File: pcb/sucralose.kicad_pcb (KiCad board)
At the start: 2 copper layers, 154.3 x 89.9 mm, 98 parts, among them M1 MountingHole_1.2mm_M1

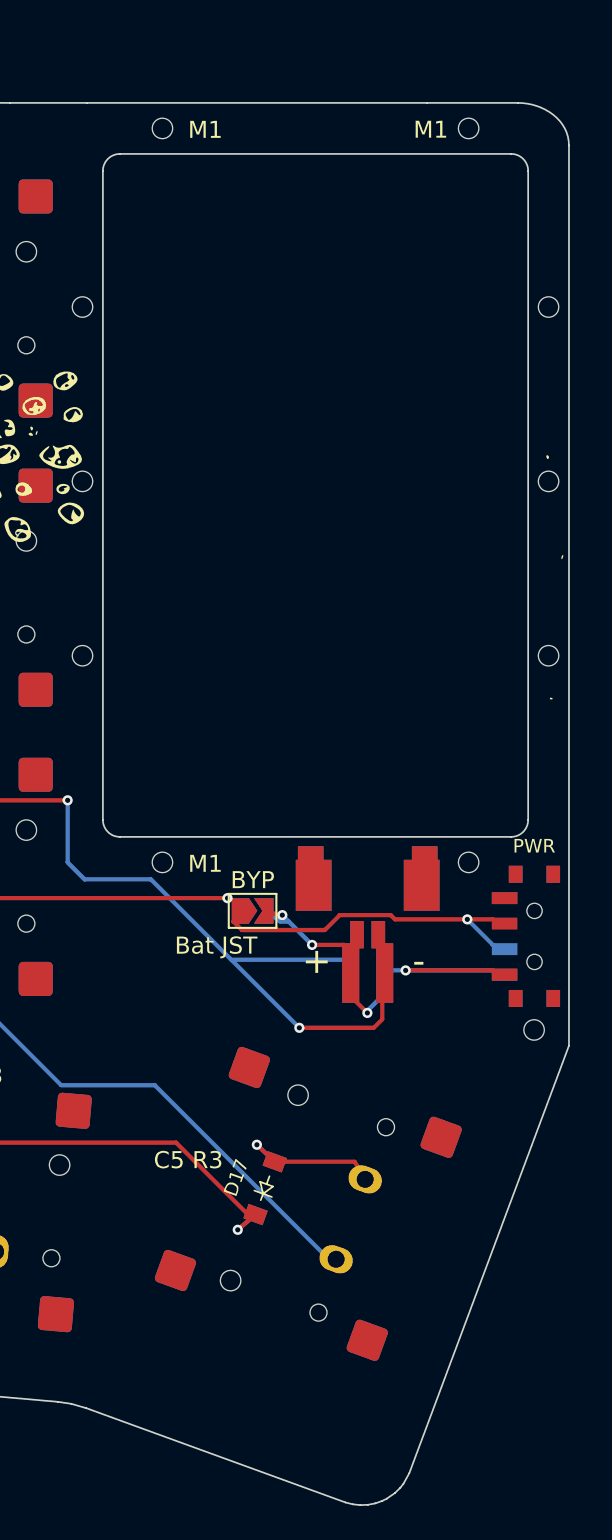
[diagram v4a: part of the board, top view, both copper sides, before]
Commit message: Battery bay cutout + 4 corner M1 holes +0.5 mm x. Right board edge, right-strip M1 holes (x 204.65), PWR switch F/B + its M1 and traces, right-strip silk art +0.5 mm with them; lower-right diagonal keeps its angle. All hole/edge gaps unchanged. DRC 362, same categories and unconnected set.
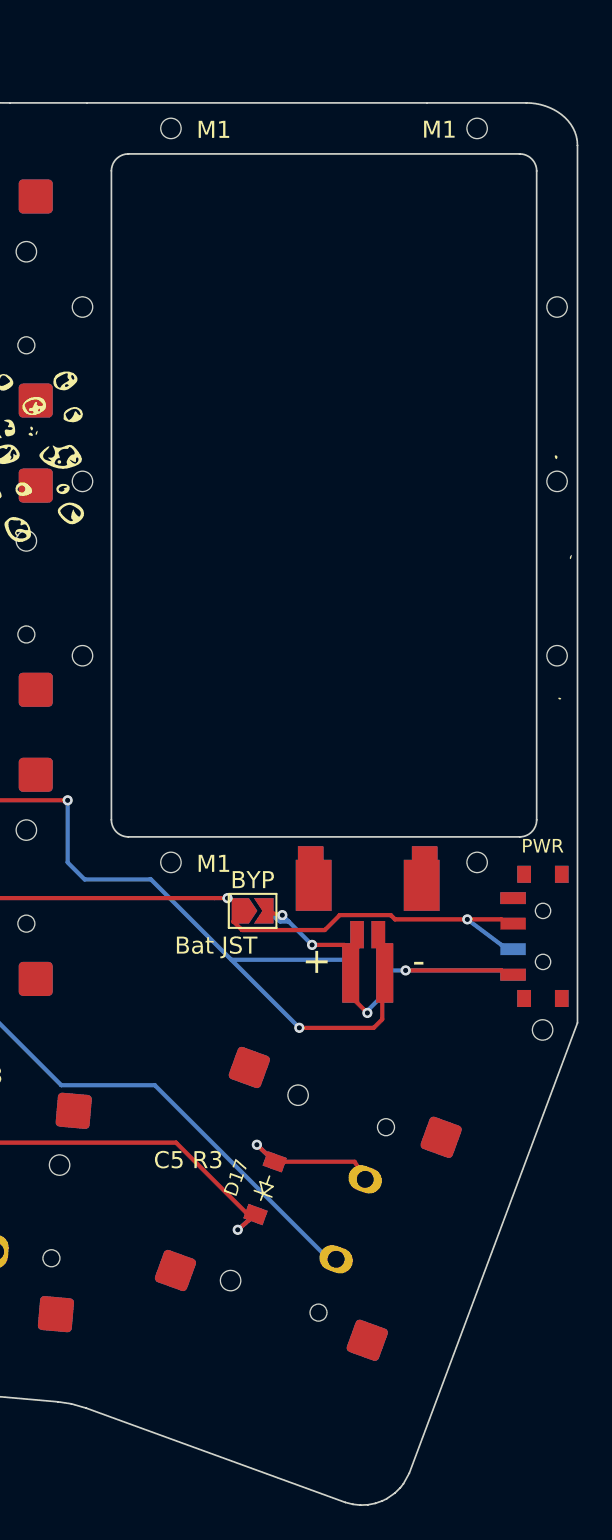
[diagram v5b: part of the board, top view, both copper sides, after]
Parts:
- moved M1 0.50 mm to (203.8, 111.0)
- moved M1 0.50 mm to (204.7, 68.5)
- moved M1 0.50 mm to (181.9, 58.0)
- moved M1 0.50 mm to (204.7, 89.0)
- moved M1 0.50 mm to (199.9, 101.2)
- moved M1 0.50 mm to (181.9, 101.2)
- moved M1 0.50 mm to (199.9, 58.0)
- moved M1 0.50 mm to (204.7, 78.8)
- moved PWR 0.50 mm to (203.8, 105.5) (x2)
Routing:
- net BAT_RAW: track 27.0 -> 28.0 mm
- net BAT_P: track 92.8 -> 93.6 mm
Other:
- board size 154.3 x 89.9 mm -> 154.8 x 89.9 mm

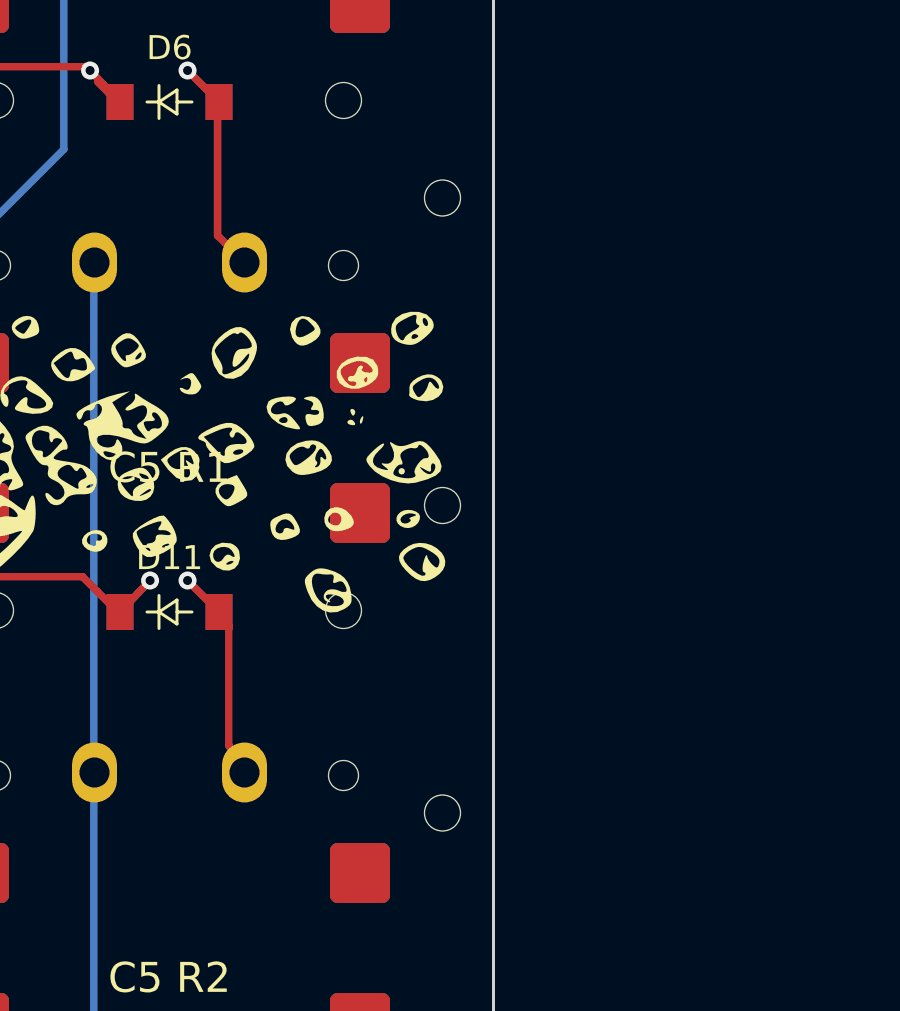
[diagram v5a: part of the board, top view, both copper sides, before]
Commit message: Left-strip battery-bay M1 holes (x 176.75 -> 177.25) +0.5 mm with the cutout; 1.2 mm to bay edge restored. DRC 362 unchanged.
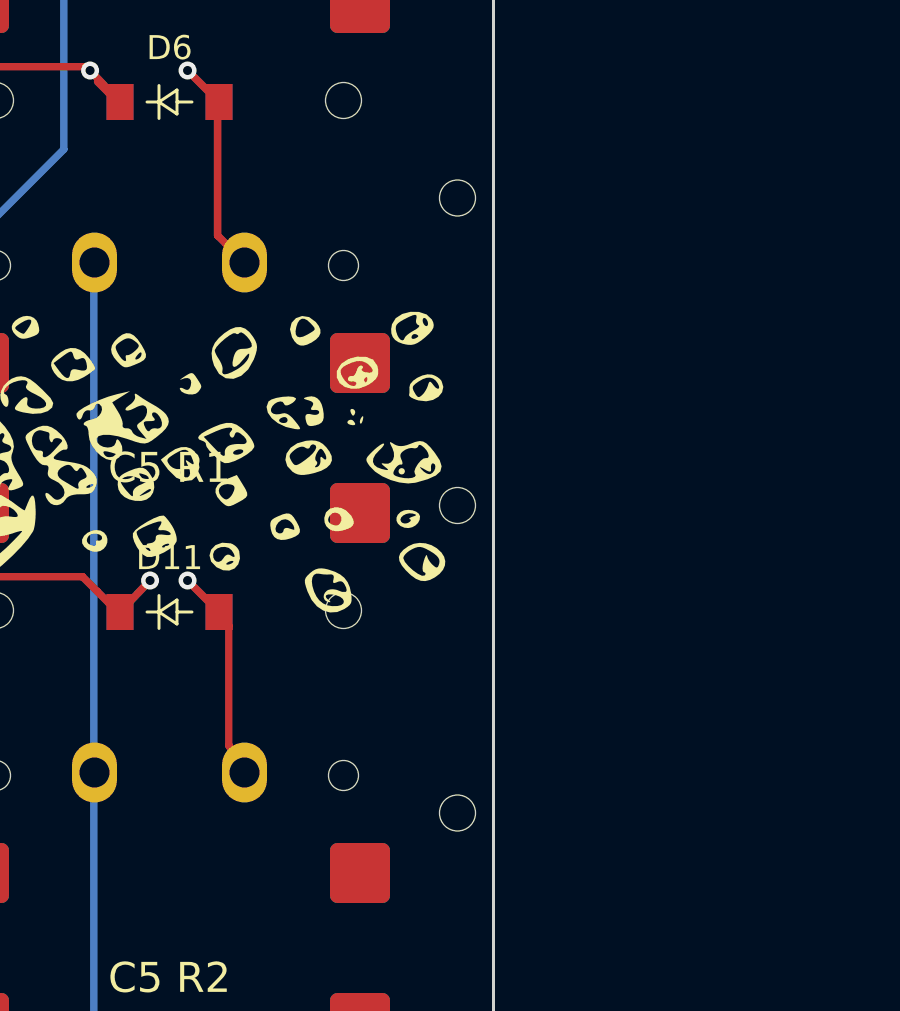
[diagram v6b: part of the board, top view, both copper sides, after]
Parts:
- moved M1 0.50 mm to (177.2, 78.8)
- moved M1 0.50 mm to (177.2, 89.0)
- moved M1 0.50 mm to (177.2, 68.5)
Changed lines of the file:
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@@
 	(footprint "CustomParts:MountingHole_1.2mm_M1"
 		(layer "F.Cu")
-		(at 176.75 68.5)
+		(at 177.25 68.5)
 		(descr "Mounting Hole 1.2mm, M1, no annular. Courtyard and head outline 2.2 mm dia (ISO 7045 / JIS B 1111 M1-M1.2 pan head dk max 2.0)")
 		(tags "mountinghole M2")
@@
 	(footprint "CustomParts:MountingHole_1.2mm_M1"
 		(layer "F.Cu")
-		(at 176.75 78.75)
+		(at 177.25 78.75)
 		(descr "Mounting Hole 1.2mm, M1, no annular. Courtyard and head outline 2.2 mm dia (ISO 7045 / JIS B 1111 M1-M1.2 pan head dk max 2.0)")
 		(tags "mountinghole M2")
@@
 	(footprint "CustomParts:MountingHole_1.2mm_M1"
 		(layer "F.Cu")
-		(at 176.75 89)
+		(at 177.25 89)
 		(descr "Mounting Hole 1.2mm, M1, no annular. Courtyard and head outline 2.2 mm dia (ISO 7045 / JIS B 1111 M1-M1.2 pan head dk max 2.0)")
 		(tags "mountinghole M2")
